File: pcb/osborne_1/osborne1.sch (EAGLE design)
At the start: 11 parts, among them J2 ATX24RH

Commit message: finishing touches
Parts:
- added LED1, LED2: (no value), SparkFun-LED:LED3MM
- added R1, R2: (no value), adafruit:R-US_0207/2V
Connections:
- new net N$3: LED1.C, R2.1
- new net N$4: LED2.C, R1.1
- net +12V: now also LED2.A
- net +5V: now also LED1.A
- net GND: now also R1.2, R2.2
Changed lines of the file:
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@@
 <part name="P+4" library="supply1" library_urn="urn:adsk.eagle:library:371" deviceset="+12V" device=""/>
 <part name="U$5" library="a" deviceset="M3_MOUNTING_HOLE" device=""/>
+<part name="LED1" library="SparkFun-LED" deviceset="LED" device="3MM"/>
+<part name="R2" library="adafruit" deviceset="R-US_" device="0207/2V"/>
+<part name="GND5" library="supply1" library_urn="urn:adsk.eagle:library:371" deviceset="GND" device=""/>
+<part name="P+7" library="supply1" library_urn="urn:adsk.eagle:library:371" deviceset="+5V" device=""/>
+<part name="LED2" library="SparkFun-LED" deviceset="LED" device="3MM"/>
+<part name="R1" library="adafruit" deviceset="R-US_" device="0207/2V"/>
+<part name="GND6" library="supply1" library_urn="urn:adsk.eagle:library:371" deviceset="GND" device=""/>
+<part name="P+8" library="supply1" library_urn="urn:adsk.eagle:library:371" deviceset="+12V" device=""/>
 </parts>
 <sheets>
@@
 </instance>
 <instance part="U$5" gate="G$1" x="-68.58" y="182.88" smashed="yes"/>
+<instance part="LED1" gate="G$1" x="-22.86" y="104.14" smashed="yes" rot="R90">
+<attribute name="NAME" x="-18.288" y="100.711" size="1.778" layer="95" font="vector" rot="R180"/>
+<attribute name="VALUE" x="-18.288" y="106.045" size="1.778" layer="96" font="vector" rot="R180" align="top-left"/>
+</instance>
+<instance part="R2" gate="G$1" x="-10.16" y="104.14" smashed="yes">
+<attribute name="NAME" x="-13.97" y="105.6386" size="1.778" layer="95"/>
+<attribute name="VALUE" x="-13.97" y="100.838" size="1.778" layer="96"/>
+</instance>
+<instance part="GND5" gate="1" x="2.54" y="101.6" smashed="yes">
+<attribute name="VALUE" x="0" y="99.06" size="1.778" layer="96"/>
+</instance>
+<instance part="P+7" gate="1" x="-30.48" y="106.68" smashed="yes">
+<attribute name="VALUE" x="-33.02" y="101.6" size="1.778" layer="96" rot="R90"/>
+</instance>
+<instance part="LED2" gate="G$1" x="-22.86" y="86.36" smashed="yes" rot="R90">
+<attribute name="NAME" x="-18.288" y="82.931" size="1.778" layer="95" font="vector" rot="R180"/>
+<attribute name="VALUE" x="-18.288" y="88.265" size="1.778" layer="96" font="vector" rot="R180" align="top-left"/>
+</instance>
+<instance part="R1" gate="G$1" x="-10.16" y="86.36" smashed="yes">
+<attribute name="NAME" x="-13.97" y="87.8586" size="1.778" layer="95"/>
+<attribute name="VALUE" x="-13.97" y="83.058" size="1.778" layer="96"/>
+</instance>
+<instance part="GND6" gate="1" x="2.54" y="83.82" smashed="yes">
+<attribute name="VALUE" x="0" y="81.28" size="1.778" layer="96"/>
+</instance>
+<instance part="P+8" gate="1" x="-30.48" y="88.9" smashed="yes" rot="MR0">
+<attribute name="VALUE" x="-27.94" y="83.82" size="1.778" layer="96" rot="MR90"/>
+</instance>
 </instances>
 <busses>
@@
 <junction x="127" y="121.92"/>
 </segment>
+<segment>
+<pinref part="R2" gate="G$1" pin="2"/>
+<pinref part="GND5" gate="1" pin="GND"/>
+<wire x1="-5.08" y1="104.14" x2="2.54" y2="104.14" width="0.1524" layer="91"/>
+</segment>
+<segment>
+<pinref part="R1" gate="G$1" pin="2"/>
+<pinref part="GND6" gate="1" pin="GND"/>
+<wire x1="-5.08" y1="86.36" x2="2.54" y2="86.36" width="0.1524" layer="91"/>
+</segment>
 </net>
 <net name="N$6" class="0">
@@
 <pinref part="P+1" gate="1" pin="+5V"/>
 </segment>
+<segment>
+<pinref part="P+7" gate="1" pin="+5V"/>
+<pinref part="LED1" gate="G$1" pin="A"/>
+<wire x1="-30.48" y1="104.14" x2="-25.4" y2="104.14" width="0.1524" layer="91"/>
+</segment>
 </net>
 <net name="N$8" class="0">
@@
 <pinref part="P+4" gate="1" pin="+12V"/>
 </segment>
+<segment>
+<pinref part="LED2" gate="G$1" pin="A"/>
+<wire x1="-30.48" y1="86.36" x2="-25.4" y2="86.36" width="0.1524" layer="91"/>
+<pinref part="P+8" gate="1" pin="+12V"/>
+</segment>
 </net>
 <net name="N$2" class="0">
@@
 </segment>
 </net>
+<net name="N$3" class="0">
+<segment>
+<pinref part="LED1" gate="G$1" pin="C"/>
+<pinref part="R2" gate="G$1" pin="1"/>
+<wire x1="-17.78" y1="104.14" x2="-15.24" y2="104.14" width="0.1524" layer="91"/>
+</segment>
+</net>
+<net name="N$4" class="0">
+<segment>
+<pinref part="LED2" gate="G$1" pin="C"/>
+<pinref part="R1" gate="G$1" pin="1"/>
+<wire x1="-17.78" y1="86.36" x2="-15.24" y2="86.36" width="0.1524" layer="91"/>
+</segment>
+</net>

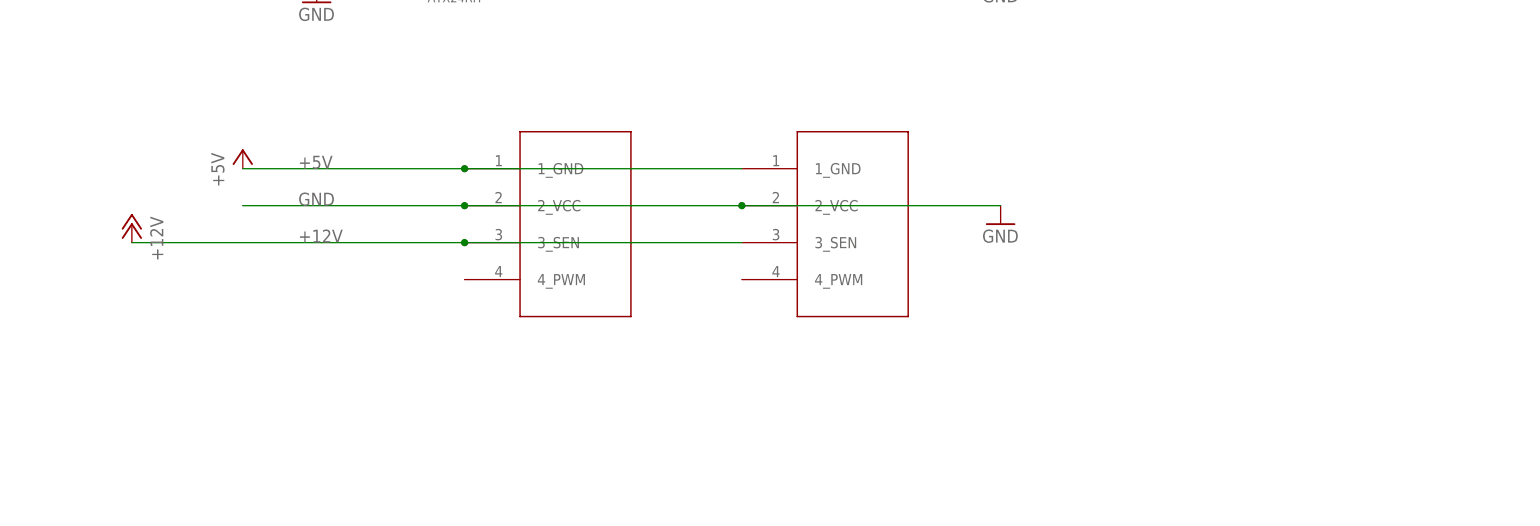
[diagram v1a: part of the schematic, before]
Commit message: added one more power connector, added decoupling cap
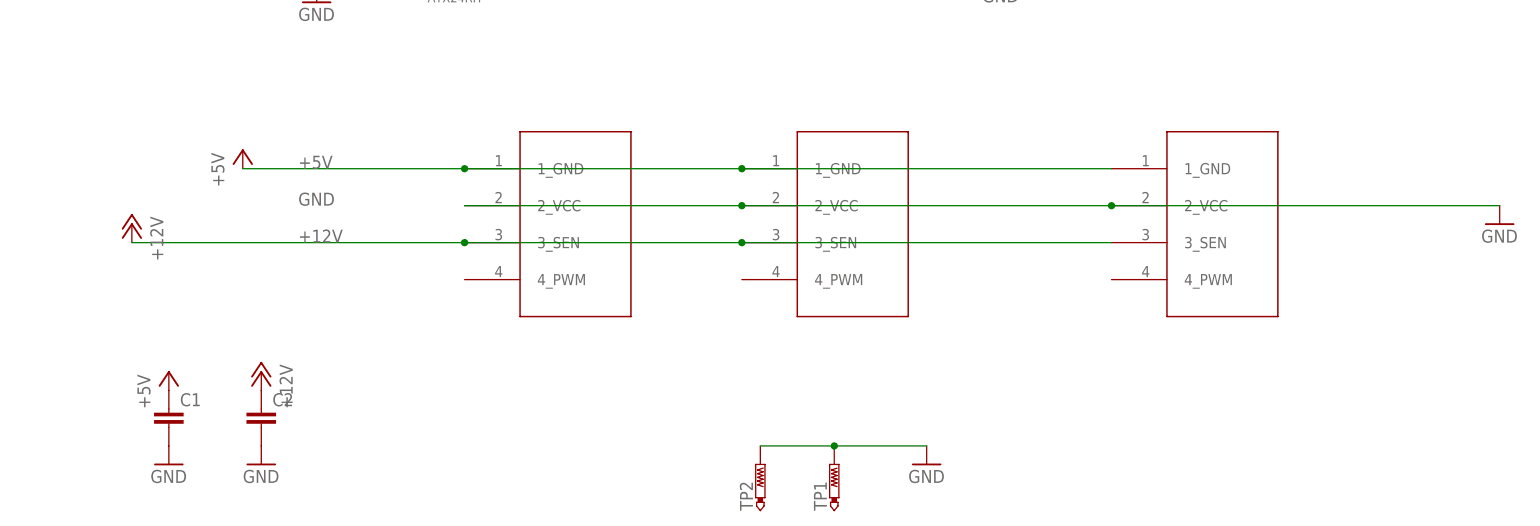
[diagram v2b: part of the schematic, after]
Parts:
- added C1, C2: (no value), capacitor-wima:C5/2.5
- added JP5: (no value), appleii:4PIN_FAN
- added TP1, TP2: PTR1PAD1-17, testpad:PTR1PAD1-17
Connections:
- net +12V: now also C2.1, JP5.3_SEN
- net +5V: now also C1.1, JP5.1_GND
- net GND: now also C1.2, C2.2, JP5.2_VCC, TP1.TP, TP2.TP
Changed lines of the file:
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@@
 <part name="GND6" library="supply1" library_urn="urn:adsk.eagle:library:371" deviceset="GND" device=""/>
 <part name="P+8" library="supply1" library_urn="urn:adsk.eagle:library:371" deviceset="+12V" device=""/>
+<part name="JP5" library="appleii" deviceset="4PIN_FAN" device=""/>
+<part name="TP1" library="testpad" library_urn="urn:adsk.eagle:library:385" deviceset="PTR1" device="PAD1-17" package3d_urn="urn:adsk.eagle:package:27949/1" value="PTR1PAD1-17"/>
+<part name="TP2" library="testpad" library_urn="urn:adsk.eagle:library:385" deviceset="PTR1" device="PAD1-17" package3d_urn="urn:adsk.eagle:package:27949/1" value="PTR1PAD1-17"/>
+<part name="GND7" library="supply1" library_urn="urn:adsk.eagle:library:371" deviceset="GND" device=""/>
+<part name="C2" library="capacitor-wima" library_urn="urn:adsk.eagle:library:116" deviceset="C" device="5/2.5" package3d_urn="urn:adsk.eagle:package:5426/1"/>
+<part name="C1" library="capacitor-wima" library_urn="urn:adsk.eagle:library:116" deviceset="C" device="5/2.5" package3d_urn="urn:adsk.eagle:package:5426/1"/>
+<part name="P+9" library="supply1" library_urn="urn:adsk.eagle:library:371" deviceset="+12V" device=""/>
+<part name="P+10" library="supply1" library_urn="urn:adsk.eagle:library:371" deviceset="+5V" device=""/>
+<part name="GND8" library="supply1" library_urn="urn:adsk.eagle:library:371" deviceset="GND" device=""/>
+<part name="GND9" library="supply1" library_urn="urn:adsk.eagle:library:371" deviceset="GND" device=""/>
 </parts>
 <sheets>
@@
 <attribute name="VALUE" x="160.02" y="149.86" size="1.778" layer="96"/>
 </instance>
-<instance part="GND3" gate="1" x="162.56" y="119.38" smashed="yes">
-<attribute name="VALUE" x="160.02" y="116.84" size="1.778" layer="96"/>
+<instance part="GND3" gate="1" x="231.14" y="119.38" smashed="yes">
+<attribute name="VALUE" x="228.6" y="116.84" size="1.778" layer="96"/>
 </instance>
 <instance part="P+1" gate="1" x="58.42" y="129.54" smashed="yes">
@@
 <instance part="P+8" gate="1" x="-30.48" y="88.9" smashed="yes" rot="MR0">
 <attribute name="VALUE" x="-27.94" y="83.82" size="1.778" layer="96" rot="MR90"/>
+</instance>
+<instance part="JP5" gate="A" x="190.5" y="119.38" smashed="yes"/>
+<instance part="TP1" gate="G$1" x="139.7" y="86.36" smashed="yes">
+<attribute name="NAME" x="138.684" y="80.01" size="1.778" layer="95" rot="R90"/>
+<attribute name="TP_SIGNAL_NAME" x="140.97" y="83.82" size="1.778" layer="97"/>
+</instance>
+<instance part="TP2" gate="G$1" x="129.54" y="86.36" smashed="yes">
+<attribute name="NAME" x="128.524" y="80.01" size="1.778" layer="95" rot="R90"/>
+<attribute name="TP_SIGNAL_NAME" x="130.81" y="83.82" size="1.778" layer="97"/>
+</instance>
+<instance part="GND7" gate="1" x="152.4" y="86.36" smashed="yes">
+<attribute name="VALUE" x="149.86" y="83.82" size="1.778" layer="96"/>
+</instance>
+<instance part="C2" gate="G$1" x="60.96" y="93.98" smashed="yes">
+<attribute name="NAME" x="62.484" y="94.361" size="1.778" layer="95"/>
+<attribute name="VALUE" x="62.484" y="89.281" size="1.778" layer="96"/>
+</instance>
+<instance part="C1" gate="G$1" x="48.26" y="93.98" smashed="yes">
+<attribute name="NAME" x="49.784" y="94.361" size="1.778" layer="95"/>
+<attribute name="VALUE" x="49.784" y="89.281" size="1.778" layer="96"/>
+</instance>
+<instance part="P+9" gate="1" x="60.96" y="99.06" smashed="yes" rot="MR0">
+<attribute name="VALUE" x="63.5" y="93.98" size="1.778" layer="96" rot="MR90"/>
+</instance>
+<instance part="P+10" gate="1" x="48.26" y="99.06" smashed="yes">
+<attribute name="VALUE" x="45.72" y="93.98" size="1.778" layer="96" rot="R90"/>
+</instance>
+<instance part="GND8" gate="1" x="60.96" y="86.36" smashed="yes">
+<attribute name="VALUE" x="58.42" y="83.82" size="1.778" layer="96"/>
+</instance>
+<instance part="GND9" gate="1" x="48.26" y="86.36" smashed="yes">
+<attribute name="VALUE" x="45.72" y="83.82" size="1.778" layer="96"/>
 </instance>
 </instances>
@@
 <segment>
 <pinref part="JP1" gate="A" pin="2_VCC"/>
-<wire x1="88.9" y1="121.92" x2="58.42" y2="121.92" width="0.1524" layer="91"/>
 <pinref part="JP2" gate="A" pin="2_VCC"/>
 <wire x1="127" y1="121.92" x2="88.9" y2="121.92" width="0.1524" layer="91"/>
-<junction x="88.9" y="121.92"/>
 <label x="66.04" y="121.92" size="1.778" layer="95"/>
 <pinref part="GND3" gate="1" pin="GND"/>
-<wire x1="127" y1="121.92" x2="162.56" y2="121.92" width="0.1524" layer="91"/>
+<wire x1="127" y1="121.92" x2="177.8" y2="121.92" width="0.1524" layer="91"/>
 <junction x="127" y="121.92"/>
+<pinref part="JP5" gate="A" pin="2_VCC"/>
+<wire x1="177.8" y1="121.92" x2="231.14" y2="121.92" width="0.1524" layer="91"/>
+<junction x="177.8" y="121.92"/>
 </segment>
 <segment>
@@
 <pinref part="GND6" gate="1" pin="GND"/>
 <wire x1="-5.08" y1="86.36" x2="2.54" y2="86.36" width="0.1524" layer="91"/>
+</segment>
+<segment>
+<pinref part="TP2" gate="G$1" pin="TP"/>
+<pinref part="TP1" gate="G$1" pin="TP"/>
+<wire x1="129.54" y1="88.9" x2="139.7" y2="88.9" width="0.1524" layer="91"/>
+<pinref part="GND7" gate="1" pin="GND"/>
+<wire x1="139.7" y1="88.9" x2="152.4" y2="88.9" width="0.1524" layer="91"/>
+<junction x="139.7" y="88.9"/>
+</segment>
+<segment>
+<pinref part="C2" gate="G$1" pin="2"/>
+<pinref part="GND8" gate="1" pin="GND"/>
+</segment>
+<segment>
+<pinref part="C1" gate="G$1" pin="2"/>
+<pinref part="GND9" gate="1" pin="GND"/>
 </segment>
 </net>
@@
 <label x="66.04" y="127" size="1.778" layer="95"/>
 <pinref part="P+1" gate="1" pin="+5V"/>
+<pinref part="JP5" gate="A" pin="1_GND"/>
+<wire x1="127" y1="127" x2="177.8" y2="127" width="0.1524" layer="91"/>
+<junction x="127" y="127"/>
 </segment>
 <segment>
@@
 <pinref part="LED1" gate="G$1" pin="A"/>
 <wire x1="-30.48" y1="104.14" x2="-25.4" y2="104.14" width="0.1524" layer="91"/>
+</segment>
+<segment>
+<pinref part="C1" gate="G$1" pin="1"/>
+<pinref part="P+10" gate="1" pin="+5V"/>
 </segment>
 </net>
@@
 <label x="66.04" y="116.84" size="1.778" layer="95"/>
 <pinref part="P+4" gate="1" pin="+12V"/>
+<pinref part="JP5" gate="A" pin="3_SEN"/>
+<wire x1="127" y1="116.84" x2="177.8" y2="116.84" width="0.1524" layer="91"/>
+<junction x="127" y="116.84"/>
 </segment>
 <segment>
@@
 <pinref part="P+8" gate="1" pin="+12V"/>
 </segment>
-</net>
+<segment>
+<pinref part="C2" gate="G$1" pin="1"/>
+<pinref part="P+9" gate="1" pin="+12V"/>
+</segment>
+</net>

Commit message: added more caps to OS1
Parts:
- removed JP4: (no value), pinhead:PINHD-1X3
- removed LED1, LED2: (no value), SparkFun-LED:LED3MM
- removed R1, R2: (no value), adafruit:R-US_0207/2V
- added C3, C5: (no value), capacitor-wima:C5/2.5
- added C4, C6: (no value), adafruit_changed:CPOL-USE3.5-8
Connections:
- removed net N$2: JP3.2_VCC, JP4.2
- removed net N$3: LED1.C, R2.1
- removed net N$4: LED2.C, R1.1
- net +12V: now also C3.1, C6.+, JP3.2_VCC; no longer JP4.1, LED2.A
- net +5V: now also C4.+, C5.1; no longer JP4.3, LED1.A
- net GND: now also C3.2, C4.-, C5.2, C6.-; no longer R1.2, R2.2
